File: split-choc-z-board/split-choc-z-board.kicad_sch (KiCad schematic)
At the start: 74 parts, among them J1 USB4105-GF-A, J2 USB4105-GF-A, SW1 SW_SPST, SW10 SW_SPST, SW11 SW_SPST, SW12 SW_SPST, SW13 SW_SPST, SW14 SW_SPST, SW15 SW_SPST, SW16 SW_SPST, SW17 SW_SPST, SW18 SW_SPST, SW19 SW_SPST, SW2 SW_SPST, SW20 SW_SPST, SW21 SW_SPST, SW22 SW_SPST, SW3 SW_SPST, SW4 SW_SPST, SW5 SW_SPST, SW6 SW_SPST, SW7 SW_SPST, SW8 SW_SPST, SW9 SW_SPST, U1 USBLC6-2SC6, U2 RP2040, U3 NCP1117-3.3_SOT223, U4 W25Q128JVS, U5 USBLC6-2SC6, X1 ABM8-272-T3

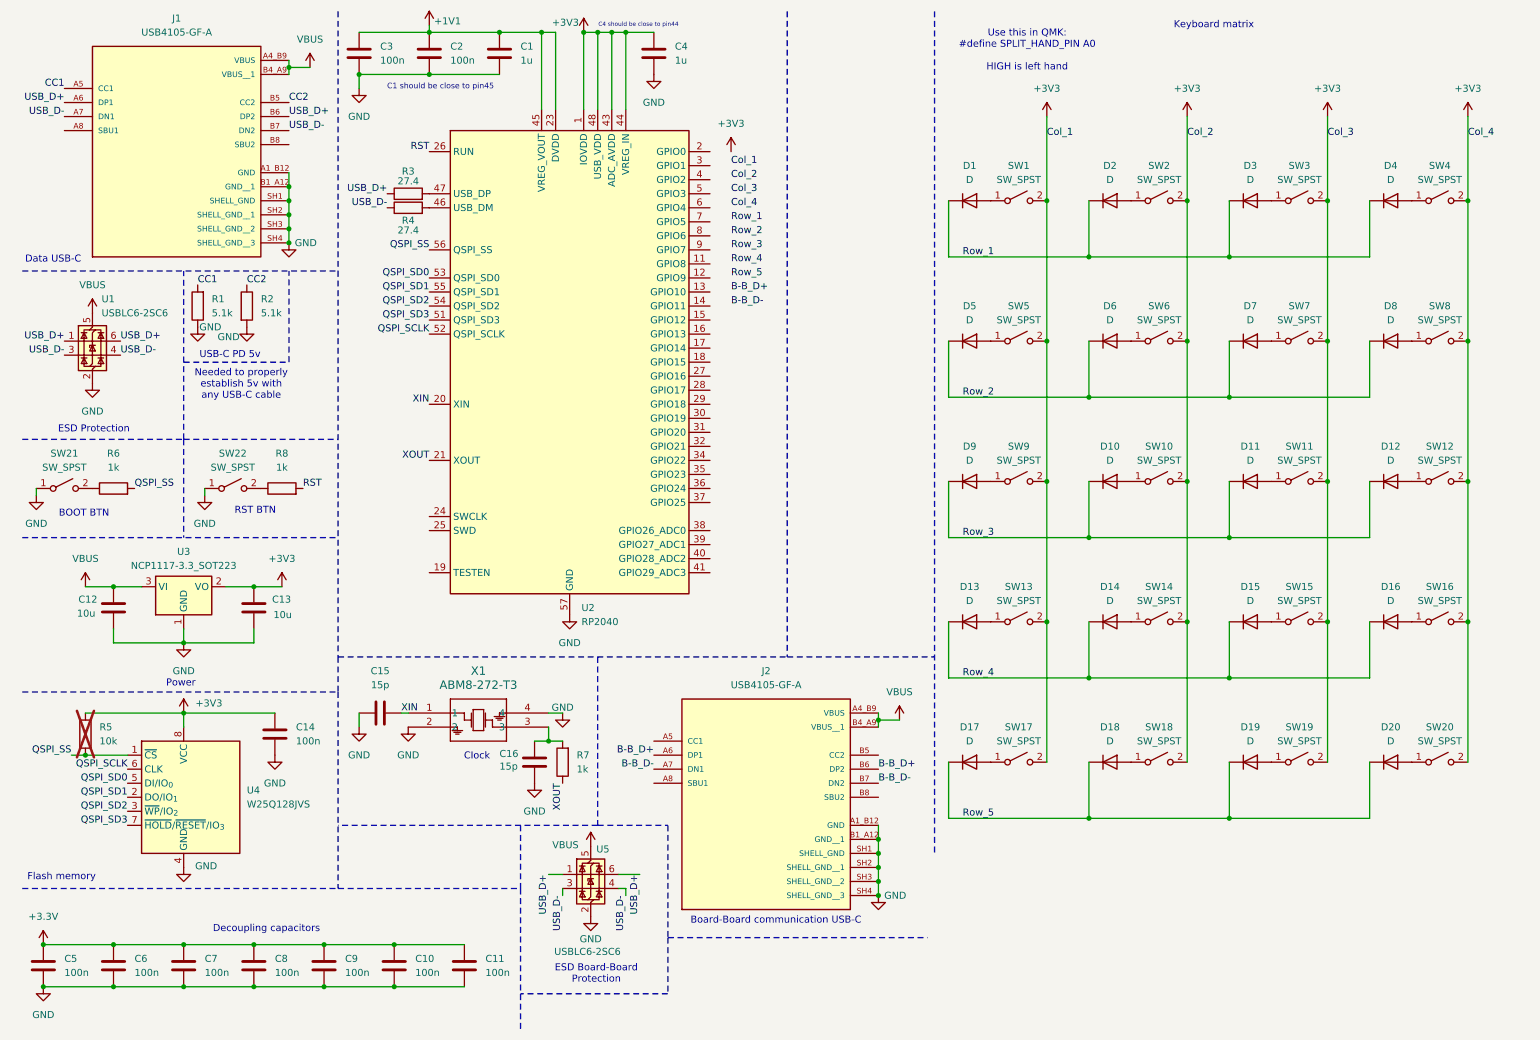
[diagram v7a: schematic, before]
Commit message: Added debug pads
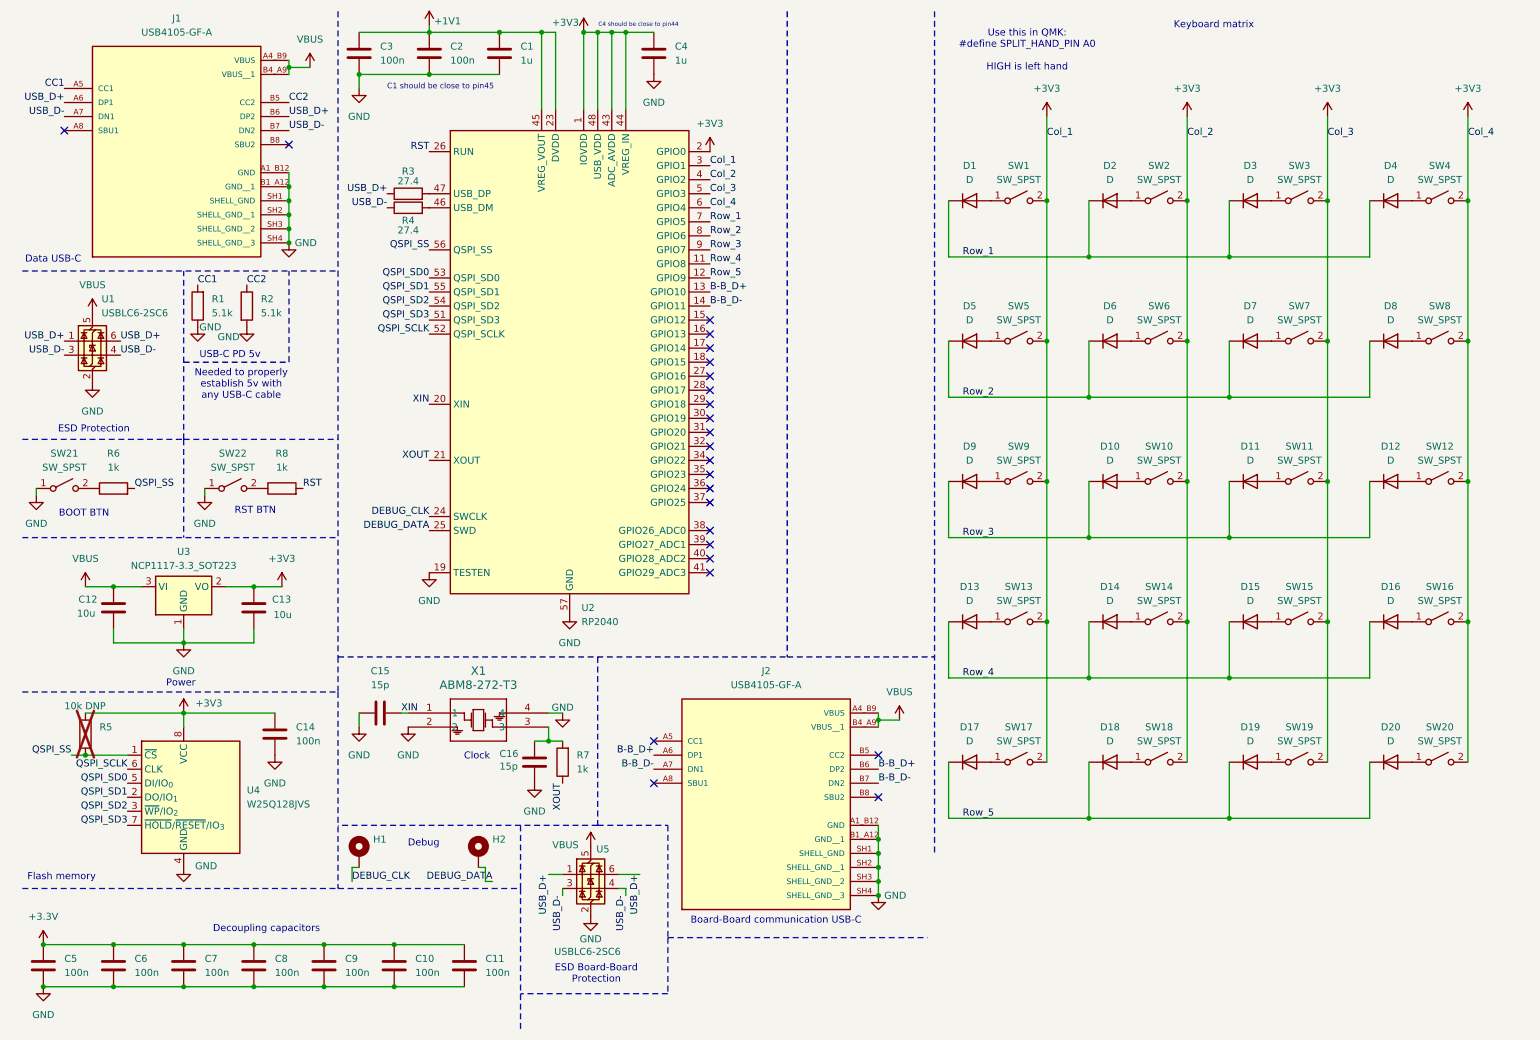
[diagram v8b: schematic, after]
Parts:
- added H1, H2: MountingHole_Pad_MP, TestPoint:TestPoint_Pad_2.0x2.0mm, symbol Mechanical:MountingHole_Pad_MP
- R5: value 10k -> 10k DNP
- SW21, SW22: footprint (none) -> Library:SW_TL3315NF250Q
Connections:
- net +3V3: now also U2.2 (GPIO0), U2.3 (GPIO1), U2.4 (GPIO2), U2.5 (GPIO3), U2.6 (GPIO4)
- net B-B_D+: now also U2.13 (GPIO10)
- net B-B_D-: now also U2.14 (GPIO11)
- net GND: now also U2.19 (TESTEN)
- net Row_1: now also U2.7 (GPIO5)
- net Row_2: now also U2.8 (GPIO6)
- net Row_3: now also U2.9 (GPIO7)
- net Row_4: now also U2.11 (GPIO8)
- net Row_5: now also U2.12 (GPIO9)
- net DEBUG_CLK: now reaches U2.24 (SWCLK)
- net DEBUG_CLK: now also H1.MP
- net DEBUG_DATA: now reaches U2.25 (SWD)
- net DEBUG_DATA: now also H2.MP
- no-connect marks 0 -> 24
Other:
- note added: "Debug"
